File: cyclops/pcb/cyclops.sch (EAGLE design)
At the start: 153 parts, among them Q1 BC817, Q2 IRF510, Q3 BC817, Q4 BC817, U1 MCP4921, U10 TLV2374, U11 THS4281, U12 MAX4564, U13 ZXTD, U14 ZXTD, U3 MAX4564, U4 LT1931, U5 LT1764A, U6 337L, U67 ZLDO1117, U69 LT1716, U7 TLV3701, U8 ADR03, U9 OP1177

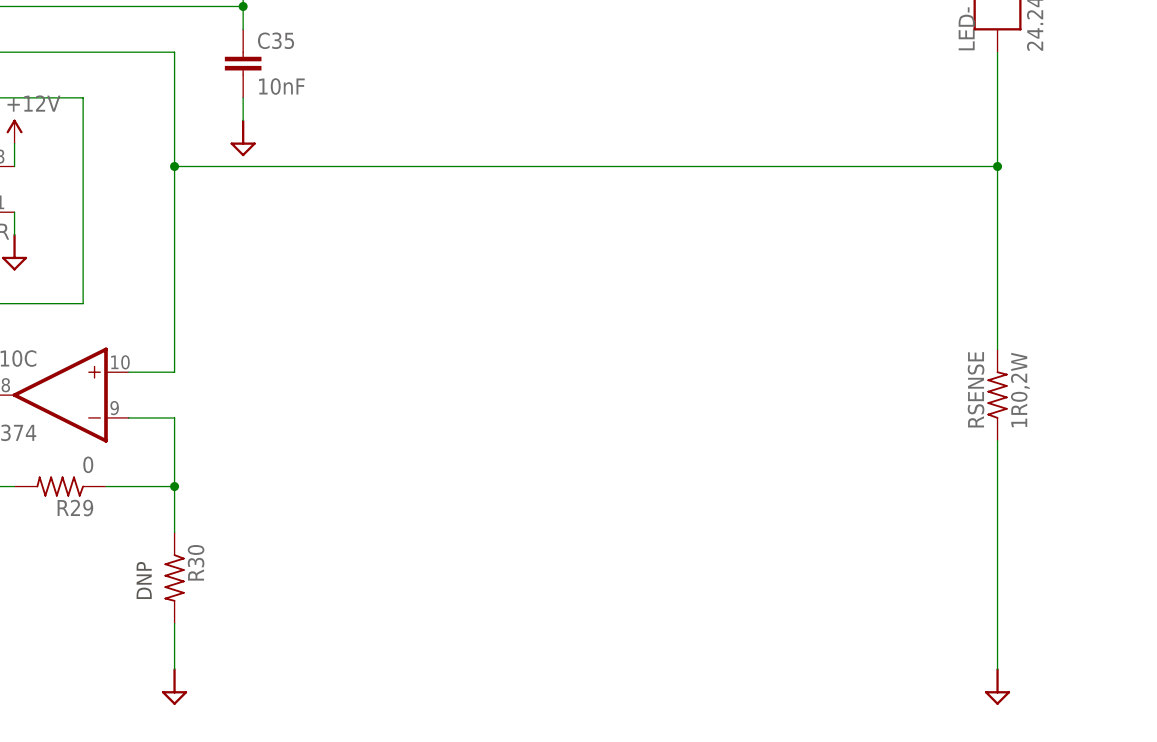
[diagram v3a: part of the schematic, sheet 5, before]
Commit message: Added some notes for the PBB refactor
- Also, added the triggered waveform example to the srce/teensy folder
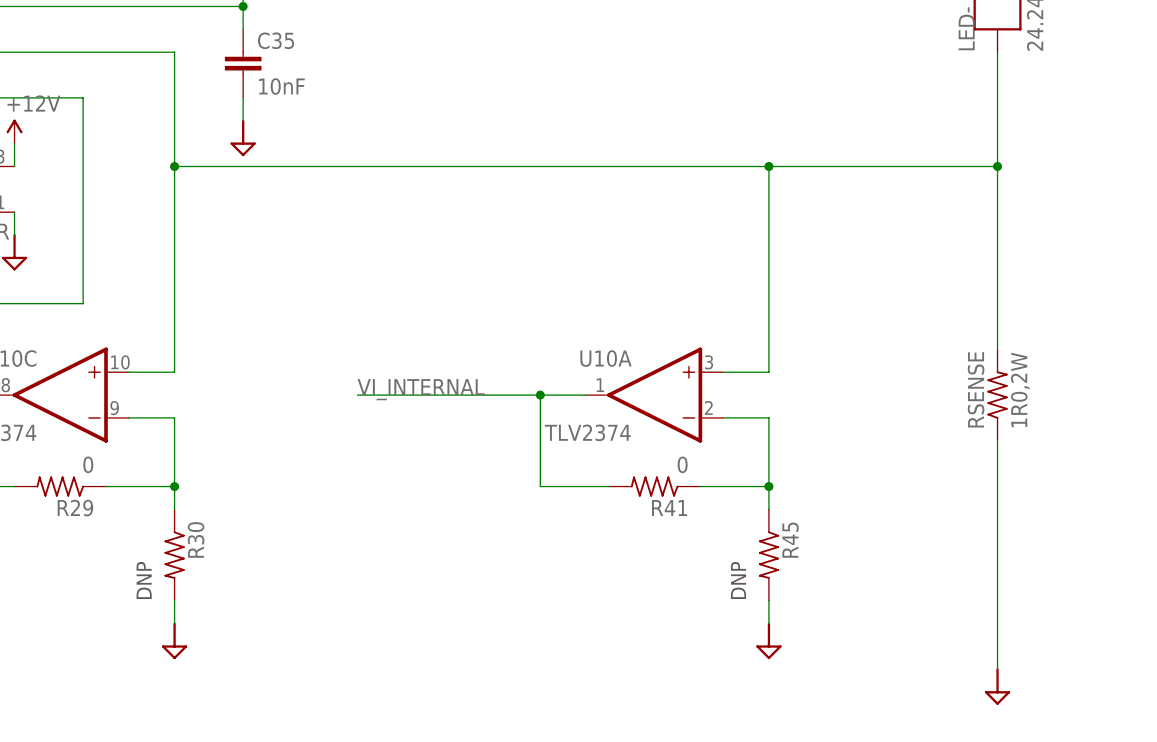
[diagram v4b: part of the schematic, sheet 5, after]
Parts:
- added R41: 0, cyclops:R_0603
- added R45: (no value), cyclops:R_0603
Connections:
- new net N$11: R41.1, R45.1, U10A.-IN
- new net VI_INTERNAL: R11.2, R3.1, R41.2, U10A.OUT, U69G$1.-IN
- net GND: now also R45.2
- net LED-: now also U10A.+IN; no longer U69G$1.-IN
- net VI: no longer R11.2, R3.1
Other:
- moved on the sheet: R30
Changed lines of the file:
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@@
 <part name="P+6" library="cyclops" deviceset="+5V" device="" value="+3V3"/>
 <part name="L1" library="cyclops" deviceset="L" device="_0603" value="MPZ1608"/>
+<part name="R41" library="cyclops" deviceset="R" device="_0603" value="0"/>
+<part name="R45" library="cyclops" deviceset="R" device="_0603"/>
+<part name="U$28" library="cyclops" deviceset="GND2" device=""/>
 </parts>
 <sheets>
@@
 6. +5V regulator layout
 7. Test LED ON circuit. You will at least have to replace the N BJT with an P BJT since LED ON is inverted.
-8. </text>
+8. Teensy itself will need to be modified with cut trace and schottky diode to work with external power
+9. Replace SMD VREF/TTL switch with vertical slide like 360‑3344‑ND</text>
 </plain>
 <instances>
@@
 <net name="VI" class="0">
 <segment>
-<pinref part="R3" gate="R" pin="1"/>
-<wire x1="101.6" y1="-2.54" x2="116.84" y2="-2.54" width="0.1524" layer="91"/>
-<wire x1="116.84" y1="-2.54" x2="116.84" y2="-38.1" width="0.1524" layer="91"/>
 <pinref part="VI" gate="G$1" pin="1"/>
 <wire x1="104.14" y1="-38.1" x2="116.84" y2="-38.1" width="0.1524" layer="91"/>
@@
 <wire x1="170.18" y1="93.98" x2="167.64" y2="93.98" width="0.1524" layer="91"/>
 <wire x1="167.64" y1="93.98" x2="167.64" y2="101.6" width="0.1524" layer="91"/>
+</segment>
+</net>
+<net name="VI_INTERNAL" class="0">
+<segment>
+<pinref part="R3" gate="R" pin="1"/>
+<wire x1="101.6" y1="-2.54" x2="116.84" y2="-2.54" width="0.1524" layer="91"/>
+<label x="111.76" y="-2.54" size="1.778" layer="95"/>
 </segment>
 </net>
@@
 </segment>
 </net>
-<net name="VI" class="0">
-<segment>
-<pinref part="R11" gate="R" pin="2"/>
-<wire x1="-99.06" y1="99.06" x2="-106.68" y2="99.06" width="0.1524" layer="91"/>
-<label x="-106.68" y="99.06" size="1.778" layer="95"/>
-</segment>
-</net>
 <net name="COMP+" class="0">
 <segment>
@@
 <pinref part="U69" gate="G$1" pin="OUT"/>
 <wire x1="-22.86" y1="-33.02" x2="-10.16" y2="-33.02" width="0.1524" layer="91"/>
-</segment>
-</net>
-<net name="LED-" class="0">
-<segment>
-<label x="-78.74" y="-35.56" size="1.778" layer="95"/>
-<wire x1="-78.74" y1="-35.56" x2="-38.1" y2="-35.56" width="0.1524" layer="91"/>
-<pinref part="U69" gate="G$1" pin="-IN"/>
 </segment>
 </net>
@@
 <wire x1="-58.42" y1="-30.48" x2="-38.1" y2="-30.48" width="0.1524" layer="91"/>
 <pinref part="U69" gate="G$1" pin="+IN"/>
+</segment>
+</net>
+<net name="VI_INTERNAL" class="0">
+<segment>
+<pinref part="R11" gate="R" pin="2"/>
+<wire x1="-99.06" y1="99.06" x2="-106.68" y2="99.06" width="0.1524" layer="91"/>
+<label x="-116.84" y="99.06" size="1.778" layer="95"/>
+</segment>
+<segment>
+<label x="-78.74" y="-35.56" size="1.778" layer="95"/>
+<wire x1="-78.74" y1="-35.56" x2="-38.1" y2="-35.56" width="0.1524" layer="91"/>
+<pinref part="U69" gate="G$1" pin="-IN"/>
 </segment>
 </net>
@@
 <text x="144.78" y="144.78" size="3.81" layer="97">DRIVETRAIN</text>
 <text x="71.12" y="-27.94" size="1.6764" layer="97" rot="R90">DNP</text>
+<text x="137.16" y="-27.94" size="1.6764" layer="97" rot="R90">DNP</text>
 </plain>
 <instances>
@@
 <instance part="U10" gate="P" x="-35.56" y="2.54"/>
 <instance part="R29" gate="R" x="60.96" y="-15.24" rot="R180"/>
-<instance part="R30" gate="R" x="73.66" y="-25.4" rot="R270"/>
+<instance part="R30" gate="R" x="73.66" y="-22.86" rot="R270"/>
 <instance part="RSENSE" gate="R" x="165.1" y="-5.08" rot="R90"/>
 <instance part="C27" gate="C" x="-17.78" y="20.32"/>
@@
 <instance part="U$24" gate="G$1" x="-25.4" y="10.16"/>
 <instance part="U$25" gate="G$1" x="-17.78" y="10.16"/>
-<instance part="U$27" gate="G$1" x="73.66" y="-38.1"/>
+<instance part="U$27" gate="G$1" x="73.66" y="-33.02"/>
 <instance part="U$29" gate="G$1" x="165.1" y="-38.1"/>
 <instance part="P-1" gate="1" x="-35.56" y="-20.32"/>
@@
 <instance part="SUPPLY12" gate="G$1" x="-35.56" y="99.06"/>
 <instance part="R37" gate="R" x="-22.86" y="86.36" rot="R90"/>
+<instance part="U10" gate="A" x="127" y="-5.08" rot="MR0"/>
+<instance part="R41" gate="R" x="127" y="-15.24" rot="R180"/>
+<instance part="R45" gate="R" x="139.7" y="-22.86" rot="R270"/>
+<instance part="U$28" gate="G$1" x="139.7" y="-33.02"/>
 </instances>
 <busses>
@@
 <pinref part="U10" gate="C" pin="+IN"/>
 <pinref part="RSENSE" gate="R" pin="2"/>
-<wire x1="73.66" y1="20.32" x2="165.1" y2="20.32" width="0.1524" layer="91"/>
+<wire x1="73.66" y1="20.32" x2="139.7" y2="20.32" width="0.1524" layer="91"/>
+<wire x1="139.7" y1="20.32" x2="165.1" y2="20.32" width="0.1524" layer="91"/>
 <wire x1="165.1" y1="20.32" x2="165.1" y2="33.02" width="0.1524" layer="91"/>
 <junction x="165.1" y="20.32"/>
@@
 <junction x="73.66" y="20.32"/>
 <pinref part="U12" gate="G$1" pin="NC"/>
+<wire x1="134.62" y1="-2.54" x2="139.7" y2="-2.54" width="0.1524" layer="91"/>
+<wire x1="139.7" y1="-2.54" x2="139.7" y2="20.32" width="0.1524" layer="91"/>
+<junction x="139.7" y="20.32"/>
+<pinref part="U10" gate="A" pin="+IN"/>
 </segment>
 </net>
@@
 <wire x1="66.04" y1="-15.24" x2="73.66" y2="-15.24" width="0.1524" layer="91"/>
 <pinref part="R30" gate="R" pin="1"/>
-<wire x1="73.66" y1="-20.32" x2="73.66" y2="-15.24" width="0.1524" layer="91"/>
+<wire x1="73.66" y1="-17.78" x2="73.66" y2="-15.24" width="0.1524" layer="91"/>
 <junction x="73.66" y="-15.24"/>
 </segment>
@@
 <segment>
 <pinref part="R30" gate="R" pin="2"/>
-<wire x1="73.66" y1="-30.48" x2="73.66" y2="-35.56" width="0.1524" layer="91"/>
+<wire x1="73.66" y1="-27.94" x2="73.66" y2="-30.48" width="0.1524" layer="91"/>
 </segment>
 <segment>
@@
 <pinref part="C36" gate="C" pin="2"/>
 <wire x1="-35.56" y1="86.36" x2="-35.56" y2="83.82" width="0.1524" layer="91"/>
+</segment>
+<segment>
+<pinref part="R45" gate="R" pin="2"/>
+<wire x1="139.7" y1="-27.94" x2="139.7" y2="-30.48" width="0.1524" layer="91"/>
 </segment>
 </net>
@@
 </segment>
 </net>
+<net name="VI_INTERNAL" class="0">
+<segment>
+<wire x1="119.38" y1="-5.08" x2="114.3" y2="-5.08" width="0.1524" layer="91"/>
+<wire x1="114.3" y1="-5.08" x2="93.98" y2="-5.08" width="0.1524" layer="91"/>
+<junction x="114.3" y="-5.08"/>
+<wire x1="114.3" y1="-5.08" x2="114.3" y2="-15.24" width="0.1524" layer="91"/>
+<pinref part="R41" gate="R" pin="2"/>
+<wire x1="114.3" y1="-15.24" x2="121.92" y2="-15.24" width="0.1524" layer="91"/>
+<pinref part="U10" gate="A" pin="OUT"/>
+<label x="93.98" y="-5.08" size="1.778" layer="95"/>
+</segment>
+</net>
+<net name="N$11" class="0">
+<segment>
+<wire x1="139.7" y1="-7.62" x2="139.7" y2="-15.24" width="0.1524" layer="91"/>
+<wire x1="139.7" y1="-7.62" x2="134.62" y2="-7.62" width="0.1524" layer="91"/>
+<pinref part="R41" gate="R" pin="1"/>
+<wire x1="132.08" y1="-15.24" x2="139.7" y2="-15.24" width="0.1524" layer="91"/>
+<pinref part="R45" gate="R" pin="1"/>
+<wire x1="139.7" y1="-17.78" x2="139.7" y2="-15.24" width="0.1524" layer="91"/>
+<junction x="139.7" y="-15.24"/>
+<pinref part="U10" gate="A" pin="-IN"/>
+</segment>
+</net>
